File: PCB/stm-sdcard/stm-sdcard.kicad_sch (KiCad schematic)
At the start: 0 parts

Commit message: weiter pcb
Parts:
- added J1, J2: Micro_SD_Card_Det1, symbol Connector:Micro_SD_Card_Det1
- added U1: STM32G431CBTx, Package_QFP:LQFP-48_7x7mm_P0.5mm, symbol MCU_ST_STM32G4:STM32G431CBTx
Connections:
- new net: U1.23 (VSS), U1.35 (VSS), U1.47 (VSS)
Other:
- title: (none) -> stm32 sdcard

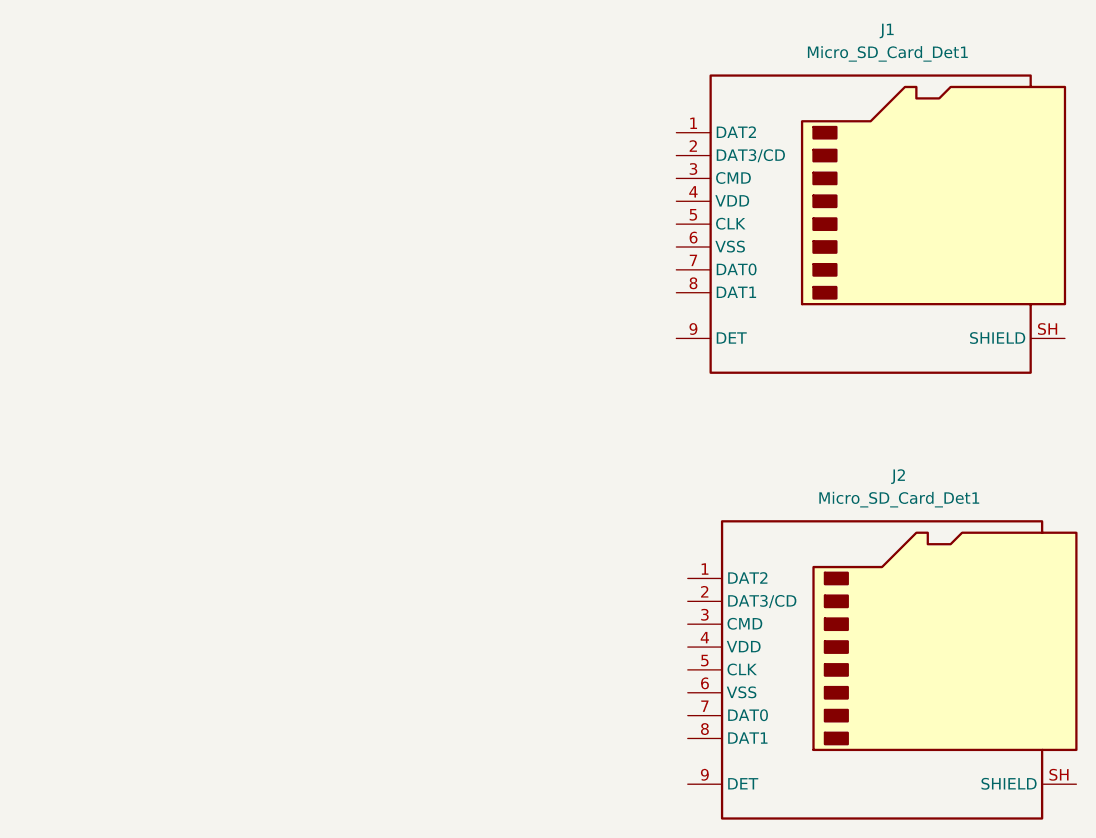
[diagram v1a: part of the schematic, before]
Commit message: added sdcard from jlc
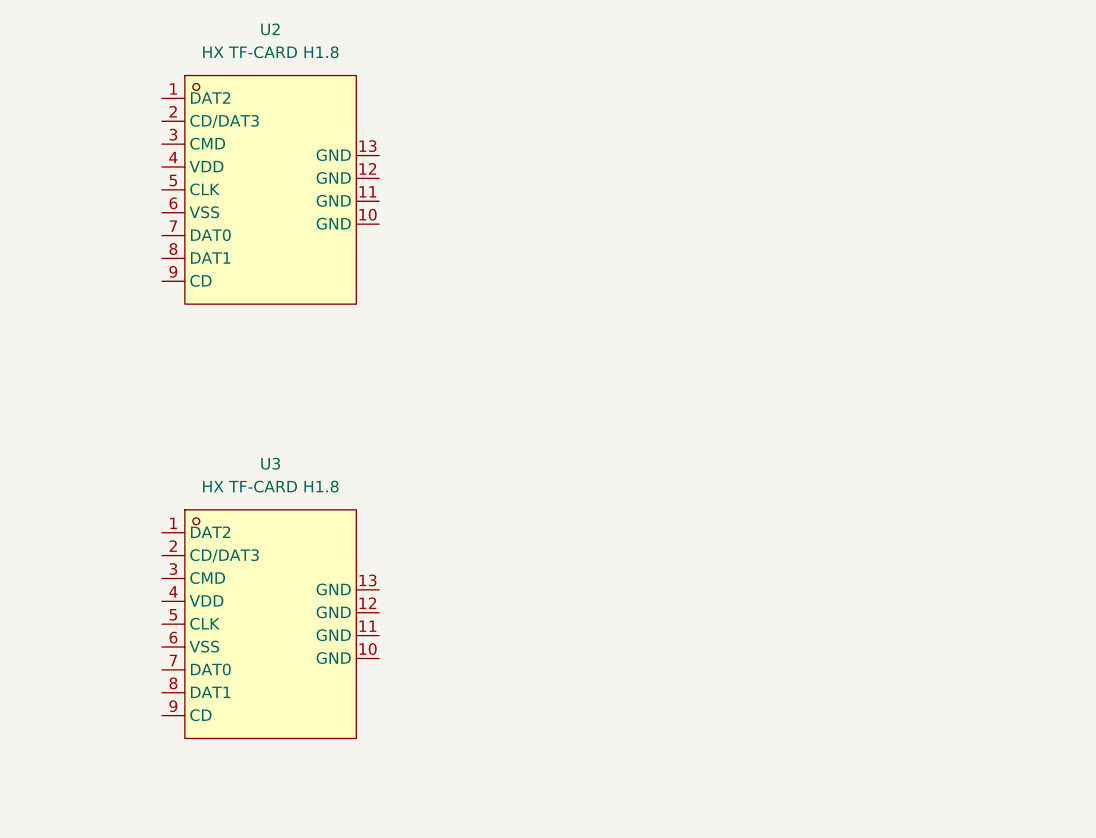
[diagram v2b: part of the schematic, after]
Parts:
- removed J1, J2: Micro_SD_Card_Det1, symbol Connector:Micro_SD_Card_Det1
- added U2, U3: HX TF-CARD H1.8, 1_hanxia_sd_slot:TF-SMD_HX-TF-CARD-H1.8-SY, symbol 1_hanxia_sd_slot:HXTF-CARDH1.8
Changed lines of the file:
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@@
 	)
 	(symbol
-		(lib_id "Connector:Micro_SD_Card_Det1")
-		(at 227.33 64.77 0)
+		(lib_id "1_hanxia_sd_slot:HXTF-CARDH1.8")
+		(at 160.02 60.96 0)
 		(unit 1)
 		(body_style 1)
@@
 		(dnp no)
 		(fields_autoplaced yes)
-		(property "Reference" "J1"
-			(at 227.965 43.18 0)
-			(show_name no)
-			(do_not_autoplace no)
-			(effects
-				(font
-					(size 1.27 1.27)
-				)
-			)
-		)
-		(property "Value" "Micro_SD_Card_Det1"
-			(at 227.965 45.72 0)
-			(show_name no)
-			(do_not_autoplace no)
-			(effects
-				(font
-					(size 1.27 1.27)
-				)
-			)
-		)
-		(property "Footprint" ""
-			(at 279.4 46.99 0)
-			(hide yes)
-			(show_name no)
-			(do_not_autoplace no)
-			(effects
-				(font
-					(size 1.27 1.27)
-				)
-			)
-		)
-		(property "Datasheet" "https://datasheet.lcsc.com/lcsc/2110151630_XKB-Connectivity-XKTF-015-N_C381082.pdf"
-			(at 227.33 62.23 0)
-			(hide yes)
-			(show_name no)
-			(do_not_autoplace no)
-			(effects
-				(font
-					(size 1.27 1.27)
-				)
-			)
-		)
-		(property "Description" "Micro SD Card Socket with one card detection pin"
-			(at 227.33 64.77 0)
-			(hide yes)
-			(show_name no)
-			(do_not_autoplace no)
-			(effects
-				(font
-					(size 1.27 1.27)
-				)
-			)
+		(property "Reference" "U2"
+			(at 159.385 43.18 0)
+			(show_name no)
+			(do_not_autoplace no)
+			(effects
+				(font
+					(size 1.27 1.27)
+				)
+			)
+		)
+		(property "Value" "HX TF-CARD H1.8"
+			(at 159.385 45.72 0)
+			(show_name no)
+			(do_not_autoplace no)
+			(effects
+				(font
+					(size 1.27 1.27)
+				)
+			)
+		)
+		(property "Footprint" "1_hanxia_sd_slot:TF-SMD_HX-TF-CARD-H1.8-SY"
+			(at 160.02 78.74 0)
+			(hide yes)
+			(show_name no)
+			(do_not_autoplace no)
+			(effects
+				(font
+					(size 1.27 1.27)
+				)
+			)
+		)
+		(property "Datasheet" "https://www.lcsc.com/datasheet/C19189036.pdf"
+			(at 160.02 81.28 0)
+			(hide yes)
+			(show_name no)
+			(do_not_autoplace no)
+			(effects
+				(font
+					(size 1.27 1.27)
+				)
+			)
+		)
+		(property "Description" ""
+			(at 160.02 60.96 0)
+			(hide yes)
+			(show_name no)
+			(do_not_autoplace no)
+			(effects
+				(font
+					(size 1.27 1.27)
+				)
+			)
+		)
+		(property "Manufacturer" "hanxia(韩下)"
+			(at 160.02 83.82 0)
+			(hide yes)
+			(show_name no)
+			(do_not_autoplace no)
+			(effects
+				(font
+					(size 1.27 1.27)
+				)
+			)
+		)
+		(property "MPN" "HX TF-CARD H1.8"
+			(at 160.02 86.36 0)
+			(hide yes)
+			(show_name no)
+			(do_not_autoplace no)
+			(effects
+				(font
+					(size 1.27 1.27)
+				)
+			)
+		)
+		(property "LCSC Part" "C19189036"
+			(at 160.02 88.9 0)
+			(hide yes)
+			(show_name no)
+			(do_not_autoplace no)
+			(effects
+				(font
+					(size 1.27 1.27)
+				)
+			)
+		)
+		(pin "13"
+		)
+		(pin "8"
+		)
+		(pin "12"
+		)
+		(pin "10"
+		)
+		(pin "1"
 		)
 		(pin "9"
 		)
+		(pin "2"
+		)
+		(pin "3"
+		)
+		(pin "4"
+		)
+		(pin "5"
+		)
+		(pin "6"
+		)
 		(pin "7"
 		)
-		(pin "5"
-		)
-		(pin "4"
-		)
-		(pin "6"
-		)
-		(pin "3"
-		)
-		(pin "2"
-		)
-		(pin "SH"
-		)
-		(pin "1"
-		)
-		(pin "8"
+		(pin "11"
 		)
 		(instances
 			(project "stm-sdcard"
 				(path "/8c3b7987-8bc9-4c61-81e1-e087d84e40be"
-					(reference "J1")
+					(reference "U2")
 					(unit 1)
 				)
@@
 	)
 	(symbol
-		(lib_id "Connector:Micro_SD_Card_Det1")
-		(at 228.6 114.3 0)
+		(lib_id "1_hanxia_sd_slot:HXTF-CARDH1.8")
+		(at 160.02 109.22 0)
 		(unit 1)
 		(body_style 1)
@@
 		(dnp no)
 		(fields_autoplaced yes)
-		(property "Reference" "J2"
-			(at 229.235 92.71 0)
-			(show_name no)
-			(do_not_autoplace no)
-			(effects
-				(font
-					(size 1.27 1.27)
-				)
-			)
-		)
-		(property "Value" "Micro_SD_Card_Det1"
-			(at 229.235 95.25 0)
-			(show_name no)
-			(do_not_autoplace no)
-			(effects
-				(font
-					(size 1.27 1.27)
-				)
-			)
-		)
-		(property "Footprint" ""
-			(at 280.67 96.52 0)
-			(hide yes)
-			(show_name no)
-			(do_not_autoplace no)
-			(effects
-				(font
-					(size 1.27 1.27)
-				)
-			)
-		)
-		(property "Datasheet" "https://datasheet.lcsc.com/lcsc/2110151630_XKB-Connectivity-XKTF-015-N_C381082.pdf"
-			(at 228.6 111.76 0)
-			(hide yes)
-			(show_name no)
-			(do_not_autoplace no)
-			(effects
-				(font
-					(size 1.27 1.27)
-				)
-			)
-		)
-		(property "Description" "Micro SD Card Socket with one card detection pin"
-			(at 228.6 114.3 0)
-			(hide yes)
-			(show_name no)
-			(do_not_autoplace no)
-			(effects
-				(font
-					(size 1.27 1.27)
-				)
-			)
+		(property "Reference" "U3"
+			(at 159.385 91.44 0)
+			(show_name no)
+			(do_not_autoplace no)
+			(effects
+				(font
+					(size 1.27 1.27)
+				)
+			)
+		)
+		(property "Value" "HX TF-CARD H1.8"
+			(at 159.385 93.98 0)
+			(show_name no)
+			(do_not_autoplace no)
+			(effects
+				(font
+					(size 1.27 1.27)
+				)
+			)
+		)
+		(property "Footprint" "1_hanxia_sd_slot:TF-SMD_HX-TF-CARD-H1.8-SY"
+			(at 160.02 127 0)
+			(hide yes)
+			(show_name no)
+			(do_not_autoplace no)
+			(effects
+				(font
+					(size 1.27 1.27)
+				)
+			)
+		)
+		(property "Datasheet" "https://www.lcsc.com/datasheet/C19189036.pdf"
+			(at 160.02 129.54 0)
+			(hide yes)
+			(show_name no)
+			(do_not_autoplace no)
+			(effects
+				(font
+					(size 1.27 1.27)
+				)
+			)
+		)
+		(property "Description" ""
+			(at 160.02 109.22 0)
+			(hide yes)
+			(show_name no)
+			(do_not_autoplace no)
+			(effects
+				(font
+					(size 1.27 1.27)
+				)
+			)
+		)
+		(property "Manufacturer" "hanxia(韩下)"
+			(at 160.02 132.08 0)
+			(hide yes)
+			(show_name no)
+			(do_not_autoplace no)
+			(effects
+				(font
+					(size 1.27 1.27)
+				)
+			)
+		)
+		(property "MPN" "HX TF-CARD H1.8"
+			(at 160.02 134.62 0)
+			(hide yes)
+			(show_name no)
+			(do_not_autoplace no)
+			(effects
+				(font
+					(size 1.27 1.27)
+				)
+			)
+		)
+		(property "LCSC Part" "C19189036"
+			(at 160.02 137.16 0)
+			(hide yes)
+			(show_name no)
+			(do_not_autoplace no)
+			(effects
+				(font
+					(size 1.27 1.27)
+				)
+			)
+		)
+		(pin "13"
+		)
+		(pin "8"
+		)
+		(pin "12"
+		)
+		(pin "10"
+		)
+		(pin "1"
 		)
 		(pin "9"
 		)
+		(pin "2"
+		)
+		(pin "3"
+		)
+		(pin "4"
+		)
+		(pin "5"
+		)
+		(pin "6"
+		)
 		(pin "7"
 		)
-		(pin "5"
-		)
-		(pin "4"
-		)
-		(pin "6"
-		)
-		(pin "3"
-		)
-		(pin "2"
-		)
-		(pin "SH"
-		)
-		(pin "1"
-		)
-		(pin "8"
+		(pin "11"
 		)
 		(instances
 			(project "stm-sdcard"
 				(path "/8c3b7987-8bc9-4c61-81e1-e087d84e40be"
-					(reference "J2")
+					(reference "U3")
 					(unit 1)
 				)

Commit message: Schaltplan almost 80% finished
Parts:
- removed U2, U3: HX TF-CARD H1.8, 1_hanxia_sd_slot:TF-SMD_HX-TF-CARD-H1.8-SY, symbol 1_hanxia_sd_slot:HXTF-CARDH1.8
- added C1: 2.2uF, symbol Device:C_Small
- added C2: 1uF, symbol Device:C_Small
- added C3, C4, C5, C6, C7, C8: 100nF, symbol Device:C_Small
- added JP1: Jumper_3_Open, symbol Jumper:Jumper_3_Open
- added R1, R2: 5k1, symbol Device:R_Small
- added R3: 20K, symbol Device:R_Small
- added SWD_PRG: Conn_01x06_Pin, symbol Connector:Conn_01x06_Pin
- added U4: TLV1117LV33DCYR, LDO-TI:SOT-223_L6.7-W3.5-P2.30-BR, symbol 3_LDO_TI:TLV1117LV33DCYR
- added UART_PRG: Conn_01x05_Pin, symbol Connector:Conn_01x05_Pin
- added USB1: TYPE-C 16P, 2_usb_C_connect:USB-C-SMD_TYPE-C16PIN_C668624, symbol 2_usb_C_connect:TYPE-C16P
- renumbered U1 to STM
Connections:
- net +3.3V: now reaches STM.1 (VBAT)
- net +3.3V: now also STM.21 (VDDA), STM.24 (VDD), STM.36 (VDD), STM.48 (VDD), C1.1, C3.1, C4.1, C5.1, C6.1, C7.1, SWD_PRG.1 (Pin_1), U4.2 (OUT), U4.4 (OUT), UART_PRG.1 (Pin_1)
- net PA2_VCP_Tx: now reaches STM.10 (PA2)
- net PA2_VCP_Tx: now also SWD_PRG.2 (Pin_2)
- net PA5: now reaches STM.13 (PA5)
- net PA6: now reaches STM.14 (PA6)
- net PA7: now reaches STM.15 (PA7)
- net GND: now reaches STM.19 (VSSA)
- net GND: now also STM.23 (VSS), STM.35 (VSS), STM.47 (VSS), C1.2, C2.2, C3.2, C4.2, C5.2, C6.2, C7.2, C8.1, R1.2, R2.2, R3.1, SWD_PRG.6 (Pin_6), U4.1 (ADJ/GND), UART_PRG.5 (Pin_5), USB1.1 (SHELL), USB1.2 (SHELL), USB1.3 (SHELL), USB1.4 (SHELL), USB1.A1B12 (GND), USB1.B1A12 (GND)
- net PA9_Tx_BOOT: now reaches STM.31 (PA9)
- net PA9_Tx_BOOT: now also UART_PRG.3 (Pin_3)
- net PA10_Rx_BOOT: now reaches STM.32 (PA10)
- net PA10_Rx_BOOT: now also UART_PRG.4 (Pin_4)
- net USB_D-: now reaches STM.33 (PA11)
- net USB_D-: now also USB1.A7 (DN1), USB1.B7 (DN2)
- net USB_D+: now reaches STM.34 (PA12)
- net USB_D+: now also USB1.A6 (DP1), USB1.B6 (DP2)
- net PA13_SWDIO: now reaches STM.37 (PA13)
- net PA13_SWDIO: now also SWD_PRG.3 (Pin_3)
- net PA14_SWDCLK: now reaches STM.38 (PA14)
- net PA14_SWDCLK: now also SWD_PRG.4 (Pin_4)
- net PB8_BOOT0: now reaches STM.45 (PB8)
- net PB8_BOOT0: now also R3.2, UART_PRG.2 (Pin_2)
- net PG10_nRST: now reaches STM.7 (PG10)
- net PG10_nRST: now also C8.2, SWD_PRG.5 (Pin_5)
- new net: R2.1, USB1.A5 (CC1)
- new net: R1.1, USB1.B5 (CC2)
- new net +5V: C2.1, JP1.2 (C), U4.3 (IN)
- new net USB_VBUS: JP1.1 (A), USB1.A4B9 (VBUS), USB1.B4A9 (VBUS)
- new net U_BAT: JP1.3 (B)
- no-connect marks 0 -> 2
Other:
- added sheet SPI-SDcard (spi.kicad_sch)

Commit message: layout almost done, error check missing, routing missing
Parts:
- added ADC1_CONN, ADC2_CONN, J2, USART1_CONN: Conn_01x03_Pin, symbol Connector:Conn_01x03_Pin
- added C9: 1uF, symbol Device:C_Small
- added DAC1_CONN, OPAMP3_OUT_CONN1: Conn_01x02_Pin, symbol Connector:Conn_01x02_Pin
- added J1: Conn_01x04_Pin, symbol Connector:Conn_01x04_Pin
- added JP2: SolderJumper_2_Bridged, symbol Jumper:SolderJumper_2_Bridged
- U4: footprint LDO-TI:SOT-223_L6.7-W3.5-P2.30-BR -> 3_LDO_TI:SOT-223_L6.7-W3.5-P2.30-BR
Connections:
- net +3.3V: now also ADC1_CONN.1 (Pin_1), ADC2_CONN.1 (Pin_1), C9.1, JP2.1 (A); no longer C3.1, C5.1, STM.1 (VBAT)
- net GND: now also ADC1_CONN.3 (Pin_3), ADC2_CONN.3 (Pin_3), C9.2, DAC1_CONN.2 (Pin_2), J1.4 (Pin_4), J2.3 (Pin_3), OPAMP3_OUT_CONN1.2 (Pin_2), USART1_CONN.3 (Pin_3)
- net PA3: now reaches STM.11 (PA3)
- net PA4_DAC1: now reaches STM.12 (PA4)
- net PA4_DAC1: now also DAC1_CONN.1 (Pin_1)
- net PB0_PU2: now reaches STM.16 (PB0)
- net PB1_OPAMP3_OUT: now reaches STM.17 (PB1)
- net PB1_OPAMP3_OUT: now also OPAMP3_OUT_CONN1.1 (Pin_1)
- net PB2_PU3: now reaches STM.18 (PB2)
- net PC13: now reaches STM.2 (PC13)
- net PC13: now also J1.3 (Pin_3)
- net at STM.20 (VREF+): now also JP2.2 (B)
- net PB10: now reaches STM.22 (PB10)
- net PB11: now reaches STM.25 (PB11)
- net PB12: now reaches STM.26 (PB12)
- net PB13: now reaches STM.27 (PB13)
- net PB14: now reaches STM.28 (PB14)
- net PB15: now reaches STM.29 (PB15)
- net PC14: now reaches STM.3 (PC14)
- net PC14: now also J1.2 (Pin_2)
- net PA8: now reaches STM.30 (PA8)
- net PA15_PU1: now reaches STM.39 (PA15)
- net PC15: now reaches STM.4 (PC15)
- net PC15: now also J1.1 (Pin_1)
- net PB3: now reaches STM.40 (PB3)
- net PB4: now reaches STM.41 (PB4)
- net PB5: now reaches STM.42 (PB5)
- net PB6_USART1_TX: now reaches STM.43 (PB6)
- net PB6_USART1_TX: now also USART1_CONN.1 (Pin_1)
- net PB6_USART1_RX: now reaches STM.44 (PB7)
- net PB6_USART1_RX: now also USART1_CONN.2 (Pin_2)
- net PB9_PU4: now reaches STM.46 (PB9)
- net PF0: now reaches STM.5 (PF0)
- net PF0: now also J2.2 (Pin_2)
- net PF1: now reaches STM.6 (PF1)
- net PF1: now also J2.1 (Pin_1)
- net PA0_ADC1: now reaches STM.8 (PA0)
- net PA0_ADC1: now also ADC1_CONN.2 (Pin_2)
- net PA1_ADC2: now reaches STM.9 (PA1)
- net PA1_ADC2: now also ADC2_CONN.2 (Pin_2)
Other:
- moved on the sheet: C1, C2, R1, R2, R3, SWD_PRG, U4, UART_PRG, USB1

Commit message: schematic finished, now footprints and routing
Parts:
- added BAT_CONN1: Conn_01x02_Pin, symbol Connector:Conn_01x02_Pin
- renumbered ADC1_CONN to ADC1_CONN1, ADC2_CONN to ADC2_CONN1, DAC1_CONN to DAC1_CONN1, STM to STM1, SWD_PRG to SWD_PRG1, UART_PRG to UART_PRG1, USART1_CONN to USART1_CONN1
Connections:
- net +3.3V: now also C3.1, C5.1, STM1.1 (VBAT)
- net GND: now also BAT_CONN1.2 (Pin_2)
- net U_BAT: now also BAT_CONN1.1 (Pin_1)
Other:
- moved on the sheet: R3

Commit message: footprints all assigned
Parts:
- ADC1_CONN1, ADC2_CONN1, J2, JP1, USART1_CONN1: footprint (none) -> Connector_PinHeader_2.54mm:PinHeader_1x03_P2.54mm_Vertical
- BAT_CONN1, DAC1_CONN1, OPAMP3_OUT_CONN1: footprint (none) -> Connector_PinHeader_2.54mm:PinHeader_1x02_P2.54mm_Vertical
- C1, C2, C3, C4, C5, C6, C7, C8, C9: footprint (none) -> Capacitor_SMD:C_0805_2012Metric_Pad1.18x1.45mm_HandSolder
- J1: footprint (none) -> Connector_PinHeader_2.54mm:PinHeader_1x04_P2.54mm_Vertical
- JP2: footprint (none) -> Jumper:SolderJumper-2_P1.3mm_Bridged_RoundedPad1.0x1.5mm
- R1, R2, R3: footprint (none) -> Resistor_SMD:R_0815_2038Metric_Pad1.20x4.05mm_HandSolder
- SWD_PRG1: footprint (none) -> Connector_PinHeader_2.54mm:PinHeader_1x06_P2.54mm_Vertical
- UART_PRG1: footprint (none) -> Connector_PinHeader_2.54mm:PinHeader_1x05_P2.54mm_Vertical
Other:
- moved on the sheet: BAT_CONN1
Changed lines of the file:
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@@
 	(wire
 		(pts
-			(xy 224.79 121.92) (xy 224.79 125.73)
+			(xy 220.98 116.84) (xy 220.98 120.65)
 		)
 		(stroke
@@
 	(wire
 		(pts
-			(xy 227.33 119.38) (xy 227.33 125.73)
+			(xy 223.52 114.3) (xy 223.52 120.65)
 		)
 		(stroke
@@
 	)
 	(label "U_BAT"
-		(at 224.79 121.92 90)
+		(at 220.98 116.84 90)
 		(effects
 			(font
@@
 			)
 		)
-		(property "Footprint" ""
+		(property "Footprint" "Resistor_SMD:R_0815_2038Metric_Pad1.20x4.05mm_HandSolder"
 			(at 267.97 87.63 0)
 			(hide yes)
@@
 			)
 		)
-		(property "Footprint" ""
+		(property "Footprint" "Capacitor_SMD:C_0805_2012Metric_Pad1.18x1.45mm_HandSolder"
 			(at 234.95 27.94 0)
 			(hide yes)
@@
 			)
 		)
-		(property "Footprint" ""
+		(property "Footprint" "Capacitor_SMD:C_0805_2012Metric_Pad1.18x1.45mm_HandSolder"
 			(at 66.04 35.56 0)
 			(hide yes)
@@
 			)
 		)
-		(property "Footprint" ""
+		(property "Footprint" "Capacitor_SMD:C_0805_2012Metric_Pad1.18x1.45mm_HandSolder"
 			(at 58.42 35.56 0)
 			(hide yes)
@@
 			)
 		)
-		(property "Footprint" ""
+		(property "Footprint" "Resistor_SMD:R_0815_2038Metric_Pad1.20x4.05mm_HandSolder"
 			(at 107.95 143.51 0)
 			(hide yes)
@@
 			)
 		)
-		(property "Footprint" ""
+		(property "Footprint" "Connector_PinHeader_2.54mm:PinHeader_1x05_P2.54mm_Vertical"
 			(at 116.84 156.21 0)
 			(hide yes)
@@
 			)
 		)
-		(property "Footprint" ""
+		(property "Footprint" "Connector_PinHeader_2.54mm:PinHeader_1x02_P2.54mm_Vertical"
 			(at 172.72 125.73 0)
 			(hide yes)
@@
 			)
 		)
-		(property "Footprint" ""
+		(property "Footprint" "Capacitor_SMD:C_0805_2012Metric_Pad1.18x1.45mm_HandSolder"
 			(at 80.01 35.56 0)
 			(hide yes)
@@
 			)
 		)
-		(property "Footprint" ""
+		(property "Footprint" "Capacitor_SMD:C_0805_2012Metric_Pad1.18x1.45mm_HandSolder"
 			(at 73.66 35.56 0)
 			(hide yes)
@@
 			)
 		)
-		(property "Footprint" ""
+		(property "Footprint" "Connector_PinHeader_2.54mm:PinHeader_1x03_P2.54mm_Vertical"
 			(at 127 120.65 0)
 			(hide yes)
@@
 			)
 		)
-		(property "Footprint" ""
+		(property "Footprint" "Resistor_SMD:R_0815_2038Metric_Pad1.20x4.05mm_HandSolder"
 			(at 267.97 77.47 0)
 			(hide yes)
@@
 			)
 		)
-		(property "Footprint" ""
+		(property "Footprint" "Connector_PinHeader_2.54mm:PinHeader_1x03_P2.54mm_Vertical"
 			(at 175.26 156.21 0)
 			(hide yes)
@@
 	(symbol
 		(lib_id "Connector:Conn_01x02_Pin")
-		(at 224.79 130.81 90)
+		(at 220.98 125.73 90)
 		(unit 1)
 		(body_style 1)
@@
 		(dnp no)
 		(property "Reference" "BAT_CONN1"
-			(at 221.996 133.35 90)
+			(at 218.186 128.27 90)
 			(show_name no)
 			(do_not_autoplace no)
@@
 		)
 		(property "Value" "Conn_01x02_Pin"
-			(at 220.218 136.398 90)
+			(at 216.408 130.81 90)
 			(show_name no)
 			(do_not_autoplace no)
@@
 			)
 		)
-		(property "Footprint" ""
-			(at 224.79 130.81 0)
+		(property "Footprint" "Connector_PinHeader_2.54mm:PinHeader_1x02_P2.54mm_Vertical"
+			(at 220.98 125.73 0)
 			(hide yes)
 			(show_name no)
@@
 		)
 		(property "Datasheet" ""
-			(at 224.79 130.81 0)
+			(at 220.98 125.73 0)
 			(hide yes)
 			(show_name no)
@@
 		)
 		(property "Description" "Generic connector, single row, 01x02, script generated"
-			(at 224.79 130.81 0)
+			(at 220.98 125.73 0)
 			(hide yes)
 			(show_name no)
@@
 			)
 		)
-		(property "Footprint" ""
+		(property "Footprint" "Connector_PinHeader_2.54mm:PinHeader_1x03_P2.54mm_Vertical"
 			(at 196.85 156.21 0)
 			(hide yes)
@@
 	(symbol
 		(lib_id "power:GND")
-		(at 227.33 119.38 180)
+		(at 223.52 114.3 180)
 		(unit 1)
 		(body_style 1)
@@
 		(dnp no)
 		(property "Reference" "#PWR060"
-			(at 227.33 113.03 0)
+			(at 223.52 107.95 0)
 			(hide yes)
 			(show_name no)
@@
 		)
 		(property "Value" "GND"
-			(at 227.33 115.062 0)
+			(at 223.52 109.982 0)
 			(show_name no)
 			(do_not_autoplace no)
@@
 		)
 		(property "Footprint" ""
-			(at 227.33 119.38 0)
+			(at 223.52 114.3 0)
 			(hide yes)
 			(show_name no)
@@
 		)
 		(property "Datasheet" ""
-			(at 227.33 119.38 0)
+			(at 223.52 114.3 0)
 			(hide yes)
 			(show_name no)
@@
 		)
 		(property "Description" "Power symbol creates a global label with name \"GND\" , ground"
-			(at 227.33 119.38 0)
+			(at 223.52 114.3 0)
 			(hide yes)
 			(show_name no)
@@
 			)
 		)
-		(property "Footprint" ""
+		(property "Footprint" "Connector_PinHeader_2.54mm:PinHeader_1x04_P2.54mm_Vertical"
 			(at 102.87 120.65 0)
 			(hide yes)
@@
 			)
 		)
-		(property "Footprint" ""
+		(property "Footprint" "Capacitor_SMD:C_0805_2012Metric_Pad1.18x1.45mm_HandSolder"
 			(at 96.52 35.56 0)
 			(hide yes)
@@
 			)
 		)
-		(property "Footprint" ""
+		(property "Footprint" "Connector_PinHeader_2.54mm:PinHeader_1x03_P2.54mm_Vertical"
 			(at 201.93 125.73 0)
 			(hide yes)
@@
 			)
 		)
-		(property "Footprint" ""
+		(property "Footprint" "Connector_PinHeader_2.54mm:PinHeader_1x06_P2.54mm_Vertical"
 			(at 147.32 156.21 0)
 			(hide yes)
@@
 			)
 		)
-		(property "Footprint" ""
+		(property "Footprint" "Capacitor_SMD:C_0805_2012Metric_Pad1.18x1.45mm_HandSolder"
 			(at 48.26 50.8 0)
 			(hide yes)
@@
 			)
 		)
-		(property "Footprint" ""
+		(property "Footprint" "Connector_PinHeader_2.54mm:PinHeader_1x02_P2.54mm_Vertical"
 			(at 147.32 125.73 0)
 			(hide yes)
@@
 			)
 		)
-		(property "Footprint" ""
+		(property "Footprint" "Connector_PinHeader_2.54mm:PinHeader_1x03_P2.54mm_Vertical"
 			(at 147.32 31.75 0)
 			(hide yes)
@@
 			)
 		)
-		(property "Footprint" ""
+		(property "Footprint" "Capacitor_SMD:C_0805_2012Metric_Pad1.18x1.45mm_HandSolder"
 			(at 86.36 35.56 0)
 			(hide yes)
@@
 			)
 		)
-		(property "Footprint" ""
+		(property "Footprint" "Capacitor_SMD:C_0805_2012Metric_Pad1.18x1.45mm_HandSolder"
 			(at 273.05 27.94 0)
 			(hide yes)
@@
 			)
 		)
-		(property "Footprint" ""
+		(property "Footprint" "Jumper:SolderJumper-2_P1.3mm_Bridged_RoundedPad1.0x1.5mm"
 			(at 105.41 39.37 0)
 			(hide yes)

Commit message: update with switches
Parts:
- added SW1, SW2: SW_Push, Button_Switch_SMD:SW_SPST_Omron_B3FS-105xP, symbol Switch:SW_Push
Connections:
- net GND: now also SW1.2, SW2.2
- net PC13: now also SW1.1
- net PC14: now also SW2.1
